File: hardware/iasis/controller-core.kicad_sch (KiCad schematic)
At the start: 39 parts, among them J1101 TSW-104-07-G-D, SW1101 PTS645SL50SMTR92LFS, SW1102 PTS645SL50SMTR92LFS, U1101 RP2354B, Y1101 ABM8-272-T3

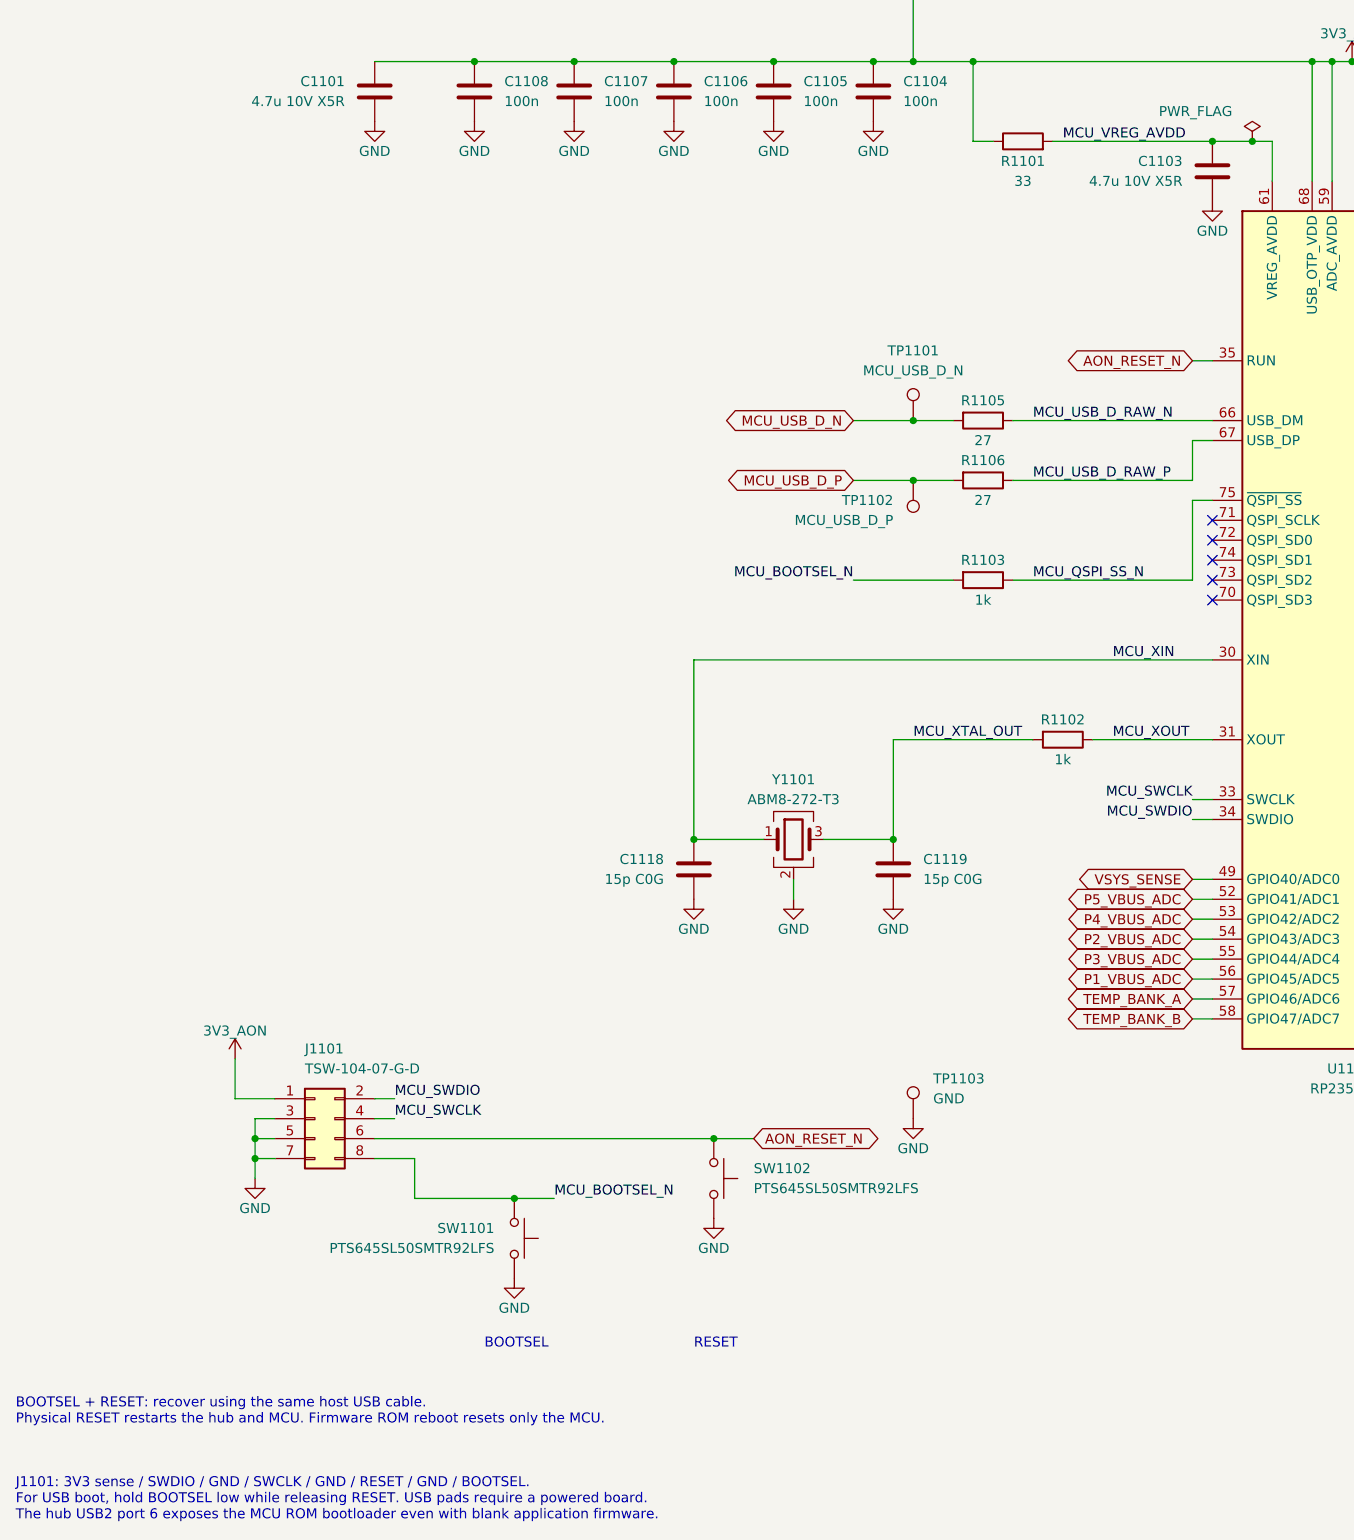
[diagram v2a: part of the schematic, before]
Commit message: Use smaller charge inductors and bulk capacitors, and solder pads for debug
The 6.8 uH PSTMAA666460 (12.5 A saturation) replaces the 10 uH 11 x 10 mm
inductor, a 6.3 mm 35 V hybrid capacitor the 10 mm 50 V bulk capacitor on
each charging buck, and an 8 mm 68 uF part the 100 uF on the charging input.
SWD and UART become three solder pads each in Raspberry Pi debug order.
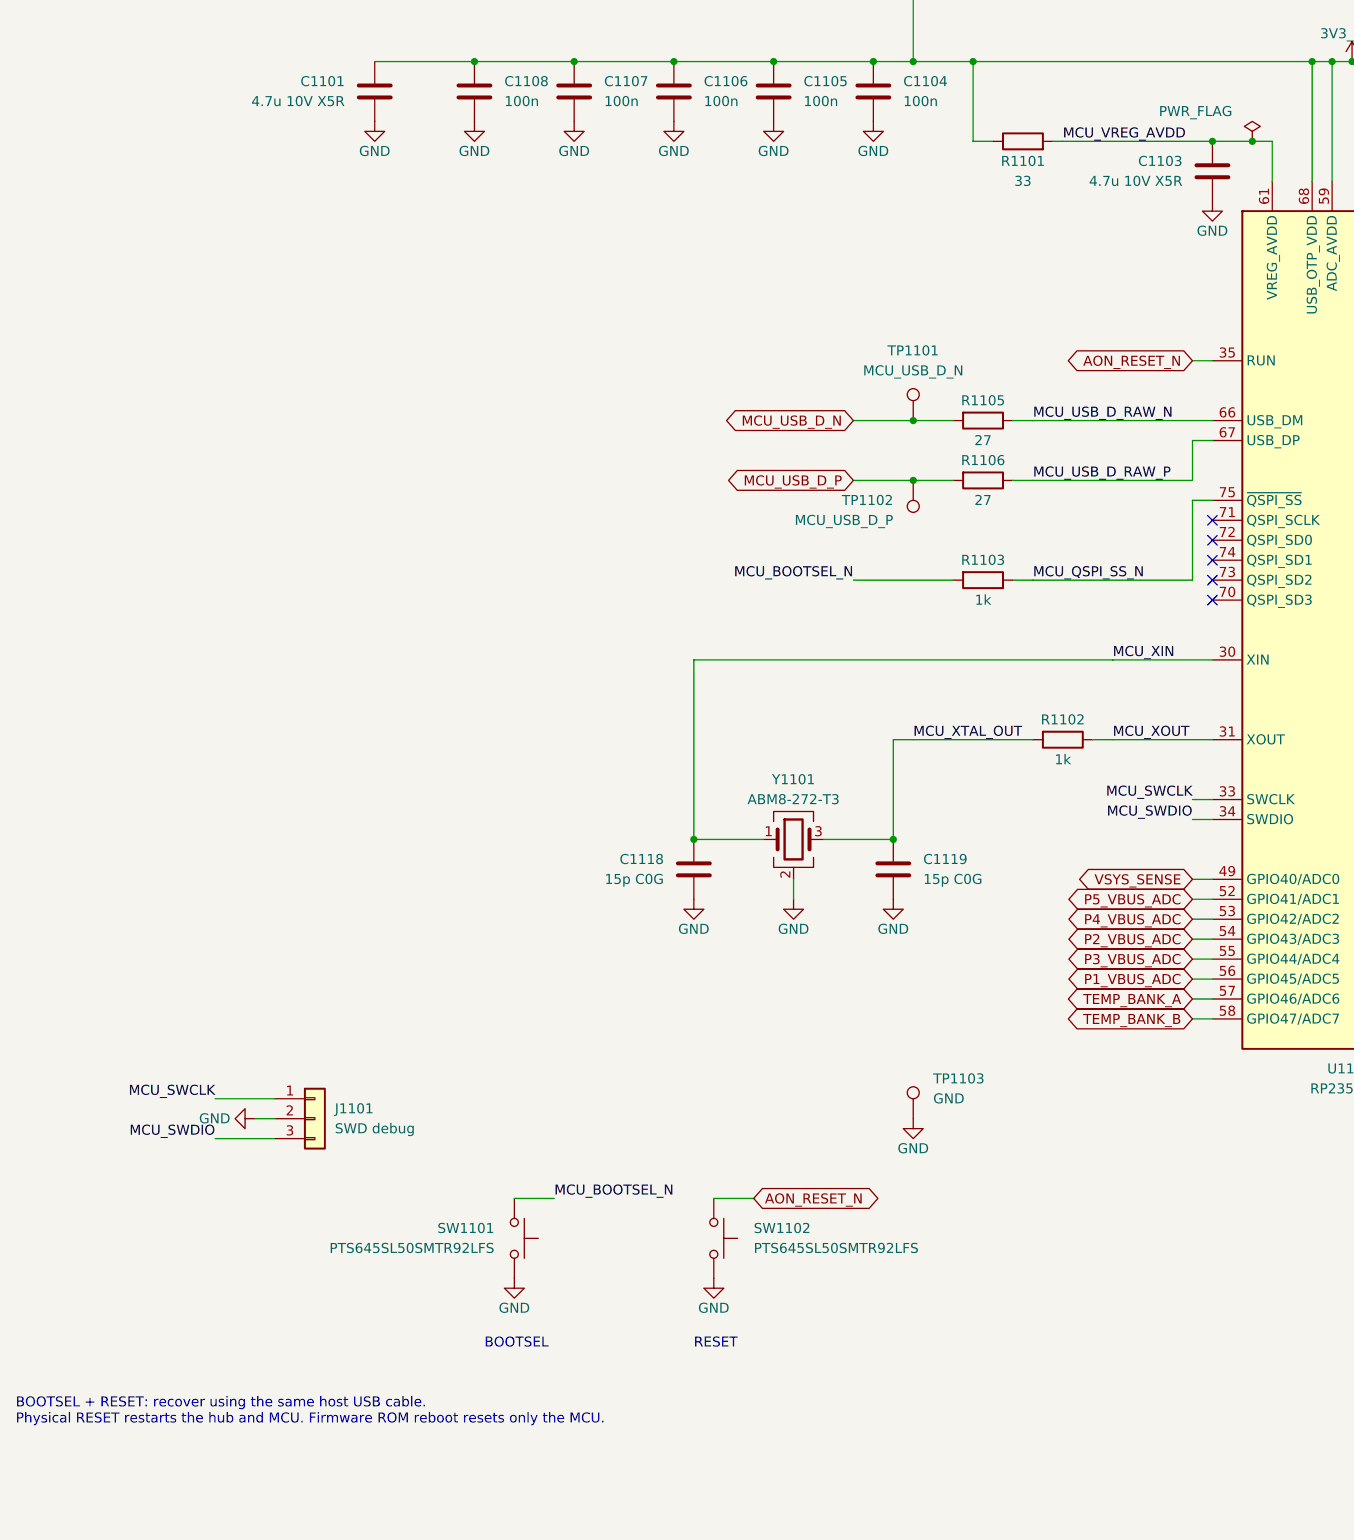
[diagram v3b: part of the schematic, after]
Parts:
- J1101: value TSW-104-07-G-D -> SWD debug; footprint Connector_PinHeader_2.54mm:PinHeader_2x04_P2.54mm_Vertical -> Iasis:SolderPads_1x03_P2.54mm; symbol Connector_Generic:Conn_02x04_Odd_Even -> Connector_Generic:Conn_01x03; AssemblyNote (none) -> Solder pads; SWCLK / GND / SWDIO; no adapter power; LCSC C3333874 -> (none); MPN TSW-104-07-G-D -> (none); Manufacturer Samtec -> (none); now left out of the parts list
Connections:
- net 3V3_AON: no longer J1101.1 (Pin_1)
- net AON_RESET_N: no longer J1101.6 (Pin_6)
- net GND: now also J1101.2 (Pin_2); no longer J1101.3 (Pin_3), J1101.5 (Pin_5), J1101.7 (Pin_7)
- net MCU_BOOTSEL_N: no longer J1101.8 (Pin_8)
- net MCU_SWCLK: now also J1101.1 (Pin_1); no longer J1101.4 (Pin_4)
- net MCU_SWDIO: now also J1101.3 (Pin_3); no longer J1101.2 (Pin_2)
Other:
- note removed: "J1101: 3V3 sense / SWDIO / GND / SWCLK / GND / RESET / GND / BOOTSEL. For USB boot, hold BOOTSEL low while releasing RESET. USB pads require a powered board. The hub USB2 port 6 exposes the MCU ROM bootloader even with blank application firmware."
- moved on the sheet: SW1102

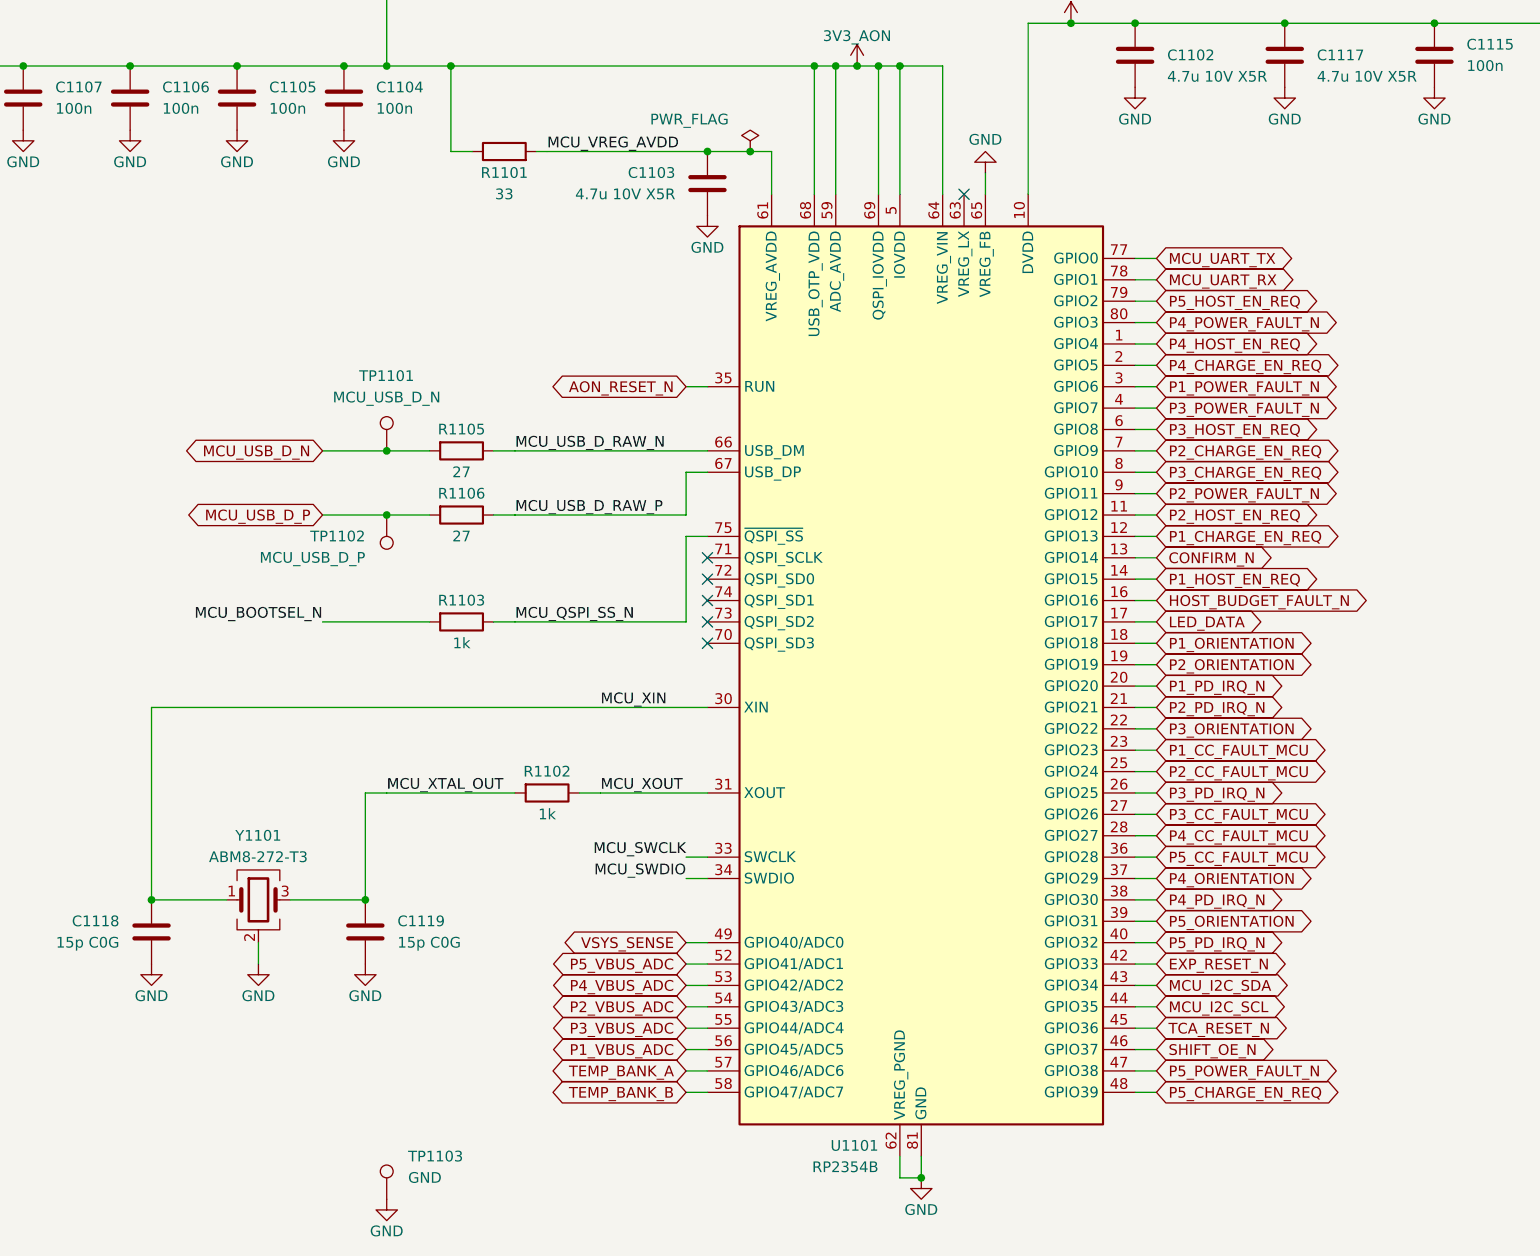
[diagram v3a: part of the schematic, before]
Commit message: Reassign RP2354 GPIOs by package side and reorder the LED chain
With the controller turned 90 degrees, charge-cell requests and faults
leave the top, upper-right and left of the package towards the charging
row, and the data-cell lines (orientation, PD interrupt, CC fault) leave
the bottom in port order. ADC channels stay on GPIO40-47, UART on
GPIO0/1, I2C on GPIO24/25.

The SK6812 chain now runs from the host LED at the front right through
ports 5 to 1, matching the board. Update PCB also adds the Hub-variant
DNP flags the swapped charging inductors and capacitors were missing.
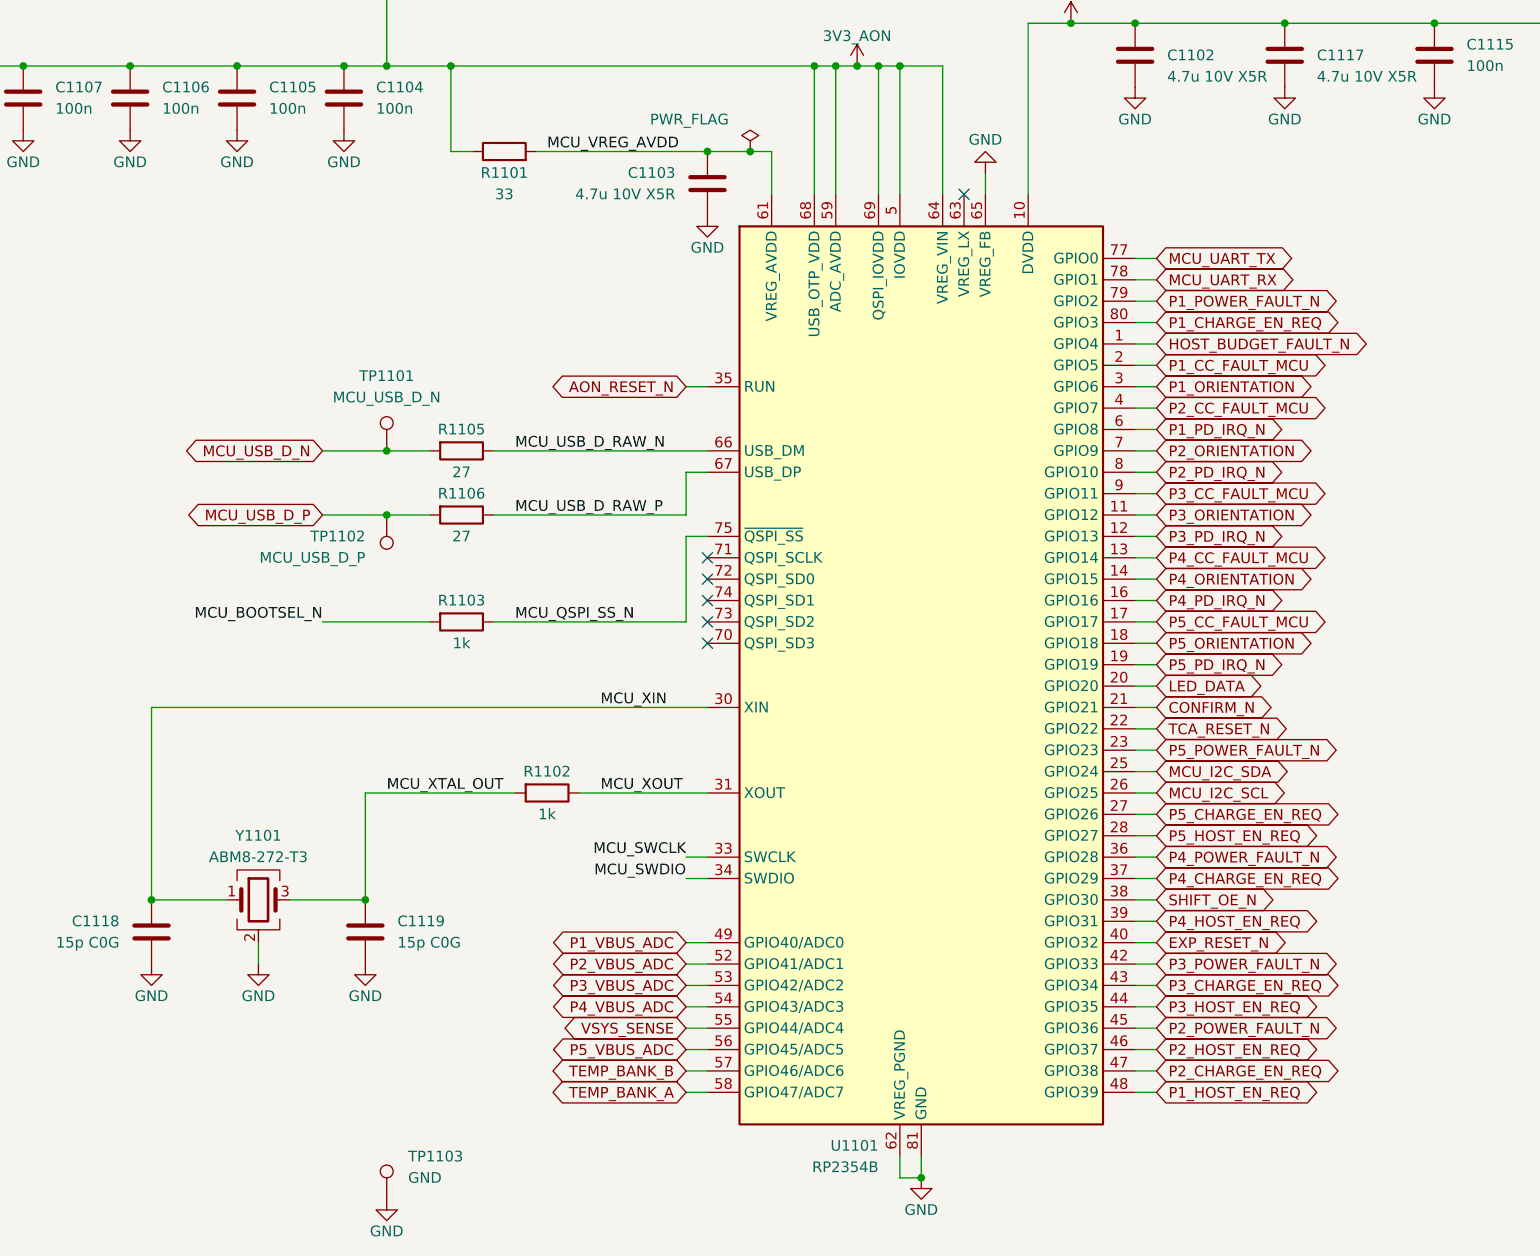
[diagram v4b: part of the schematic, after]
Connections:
- net CONFIRM_N: now also U1101.21 (GPIO21); no longer U1101.13 (GPIO14)
- net EXP_RESET_N: now also U1101.40 (GPIO32); no longer U1101.42 (GPIO33)
- net HOST_BUDGET_FAULT_N: now also U1101.1 (GPIO4); no longer U1101.16 (GPIO16)
- net LED_DATA: now also U1101.20 (GPIO20); no longer U1101.17 (GPIO17)
- net MCU_I2C_SCL: now also U1101.26 (GPIO25); no longer U1101.44 (GPIO35)
- net MCU_I2C_SDA: now also U1101.25 (GPIO24); no longer U1101.43 (GPIO34)
- net P1_CC_FAULT_MCU: now also U1101.2 (GPIO5); no longer U1101.23 (GPIO23)
- net P1_CHARGE_EN_REQ: now also U1101.80 (GPIO3); no longer U1101.12 (GPIO13)
- net P1_HOST_EN_REQ: now also U1101.48 (GPIO39); no longer U1101.14 (GPIO15)
- net P1_ORIENTATION: now also U1101.3 (GPIO6); no longer U1101.18 (GPIO18)
- net P1_PD_IRQ_N: now also U1101.6 (GPIO8); no longer U1101.20 (GPIO20)
- net P1_POWER_FAULT_N: now also U1101.79 (GPIO2); no longer U1101.3 (GPIO6)
- net P1_VBUS_ADC: now also U1101.49 (GPIO40/ADC0); no longer U1101.56 (GPIO45/ADC5)
- net P2_CC_FAULT_MCU: now also U1101.4 (GPIO7); no longer U1101.25 (GPIO24)
- net P2_CHARGE_EN_REQ: now also U1101.47 (GPIO38); no longer U1101.7 (GPIO9)
- net P2_HOST_EN_REQ: now also U1101.46 (GPIO37); no longer U1101.11 (GPIO12)
- net P2_ORIENTATION: now also U1101.7 (GPIO9); no longer U1101.19 (GPIO19)
- net P2_PD_IRQ_N: now also U1101.8 (GPIO10); no longer U1101.21 (GPIO21)
- net P2_POWER_FAULT_N: now also U1101.45 (GPIO36); no longer U1101.9 (GPIO11)
- net P2_VBUS_ADC: now also U1101.52 (GPIO41/ADC1); no longer U1101.54 (GPIO43/ADC3)
- net P3_CC_FAULT_MCU: now also U1101.9 (GPIO11); no longer U1101.27 (GPIO26)
- net P3_CHARGE_EN_REQ: now also U1101.43 (GPIO34); no longer U1101.8 (GPIO10)
- net P3_HOST_EN_REQ: now also U1101.44 (GPIO35); no longer U1101.6 (GPIO8)
- net P3_ORIENTATION: now also U1101.11 (GPIO12); no longer U1101.22 (GPIO22)
- net P3_PD_IRQ_N: now also U1101.12 (GPIO13); no longer U1101.26 (GPIO25)
- net P3_POWER_FAULT_N: now also U1101.42 (GPIO33); no longer U1101.4 (GPIO7)
- net P3_VBUS_ADC: now also U1101.53 (GPIO42/ADC2); no longer U1101.55 (GPIO44/ADC4)
- net P4_CC_FAULT_MCU: now also U1101.13 (GPIO14); no longer U1101.28 (GPIO27)
- net P4_CHARGE_EN_REQ: now also U1101.37 (GPIO29); no longer U1101.2 (GPIO5)
- net P4_HOST_EN_REQ: now also U1101.39 (GPIO31); no longer U1101.1 (GPIO4)
- net P4_ORIENTATION: now also U1101.14 (GPIO15); no longer U1101.37 (GPIO29)
- net P4_PD_IRQ_N: now also U1101.16 (GPIO16); no longer U1101.38 (GPIO30)
- net P4_POWER_FAULT_N: now also U1101.36 (GPIO28); no longer U1101.80 (GPIO3)
- net P4_VBUS_ADC: now also U1101.54 (GPIO43/ADC3); no longer U1101.53 (GPIO42/ADC2)
- net P5_CC_FAULT_MCU: now also U1101.17 (GPIO17); no longer U1101.36 (GPIO28)
- net P5_CHARGE_EN_REQ: now also U1101.27 (GPIO26); no longer U1101.48 (GPIO39)
- net P5_HOST_EN_REQ: now also U1101.28 (GPIO27); no longer U1101.79 (GPIO2)
- net P5_ORIENTATION: now also U1101.18 (GPIO18); no longer U1101.39 (GPIO31)
- net P5_PD_IRQ_N: now also U1101.19 (GPIO19); no longer U1101.40 (GPIO32)
- net P5_POWER_FAULT_N: now also U1101.23 (GPIO23); no longer U1101.47 (GPIO38)
- net P5_VBUS_ADC: now also U1101.56 (GPIO45/ADC5); no longer U1101.52 (GPIO41/ADC1)
- net SHIFT_OE_N: now also U1101.38 (GPIO30); no longer U1101.46 (GPIO37)
- net TCA_RESET_N: now also U1101.22 (GPIO22); no longer U1101.45 (GPIO36)
- net TEMP_BANK_A: now also U1101.58 (GPIO47/ADC7); no longer U1101.57 (GPIO46/ADC6)
- net TEMP_BANK_B: now also U1101.57 (GPIO46/ADC6); no longer U1101.58 (GPIO47/ADC7)
- net VSYS_SENSE: now also U1101.55 (GPIO44/ADC4); no longer U1101.49 (GPIO40/ADC0)
